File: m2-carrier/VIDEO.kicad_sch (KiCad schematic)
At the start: 8 parts, among them U7 AT7456E

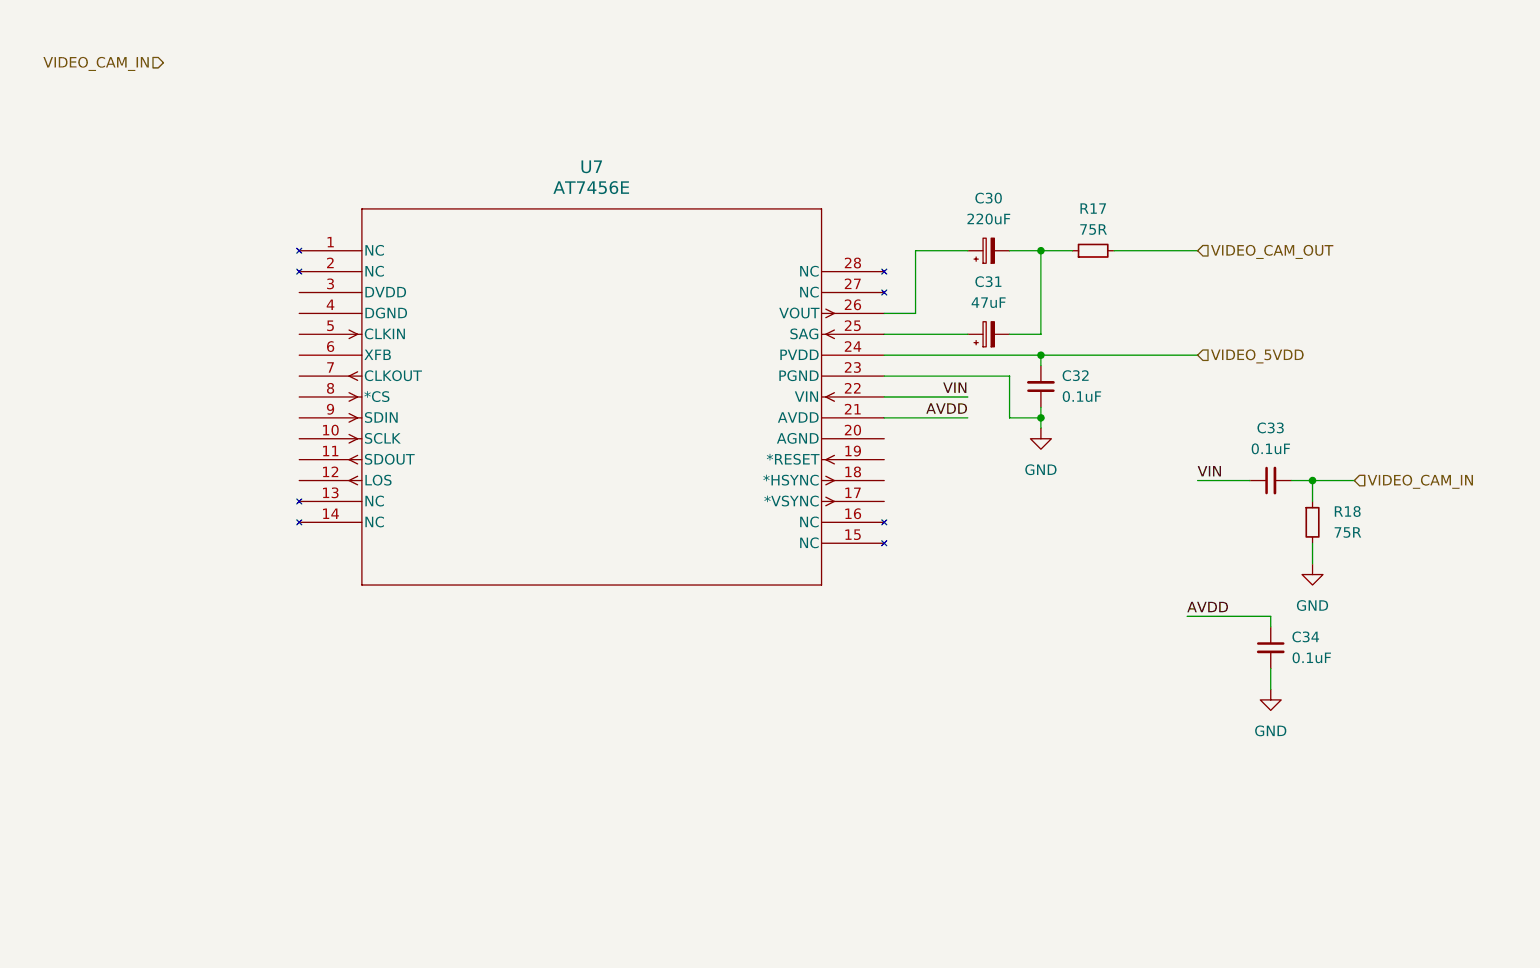
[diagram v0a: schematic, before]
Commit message: Populated OSD IC
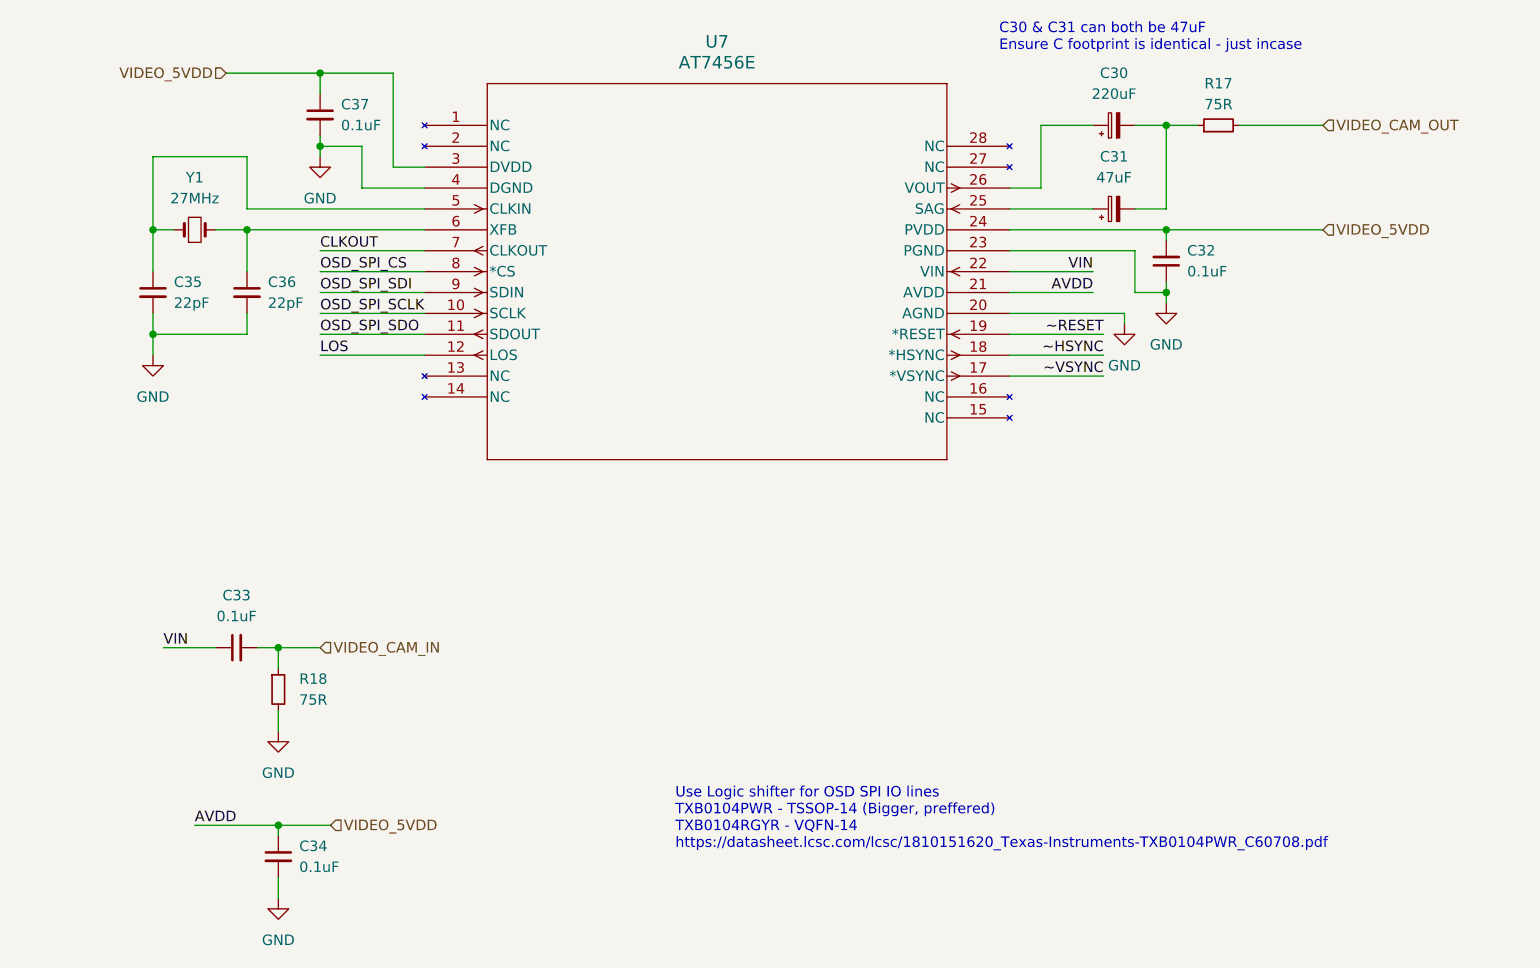
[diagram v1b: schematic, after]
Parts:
- added C35, C36: 22pF, symbol Device:C_Small
- added C37: 0.1uF, symbol Device:C_Small
- added Y1: 27MHz, symbol Device:Crystal_Small
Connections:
- net AVDD is gone; now on net VIDEO_5VDD: C34.1, U7.21 (AVDD)
- net GND: now also U7.20 (AGND), U7.4 (DGND), C35.2, C36.2, C37.2
- net VIDEO_5VDD: now also U7.3 (DVDD), C37.1
- net OSD_SPI_SCLK: now reaches U7.10 (SCLK)
- net OSD_SPI_SDO: now reaches U7.11 (SDOUT)
- net LOS: now reaches U7.12 (LOS)
- net ~VSYNC: now reaches U7.17 (*VSYNC)
- net ~HSYNC: now reaches U7.18 (*HSYNC)
- net ~RESET: now reaches U7.19 (*RESET)
- net at U7.5 (CLKIN): now also C35.1, Y1.1
- net at U7.6 (XFB): now also C36.1, Y1.2
- net CLKOUT: now reaches U7.7 (CLKOUT)
- net OSD_SPI_CS: now reaches U7.8 (*CS)
- net OSD_SPI_SDI: now reaches U7.9 (SDIN)
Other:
- note added: "C30 & C31 can both be 47uF Ensure C footprint is identical - just incase"
- note added: "Use Logic shifter for OSD SPI IO lines TXB0104PWR - TSSOP-14 (Bigger, preffered) TXB0104RGYR - VQFN-14 https://datasheet.lcsc.com/lcsc/1810151620_Texas-Instruments-TXB0104PWR_C60708.pdf"
- moved on the sheet: C30, C31, C32, C33, C34, R17, R18, U7

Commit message: Added base board
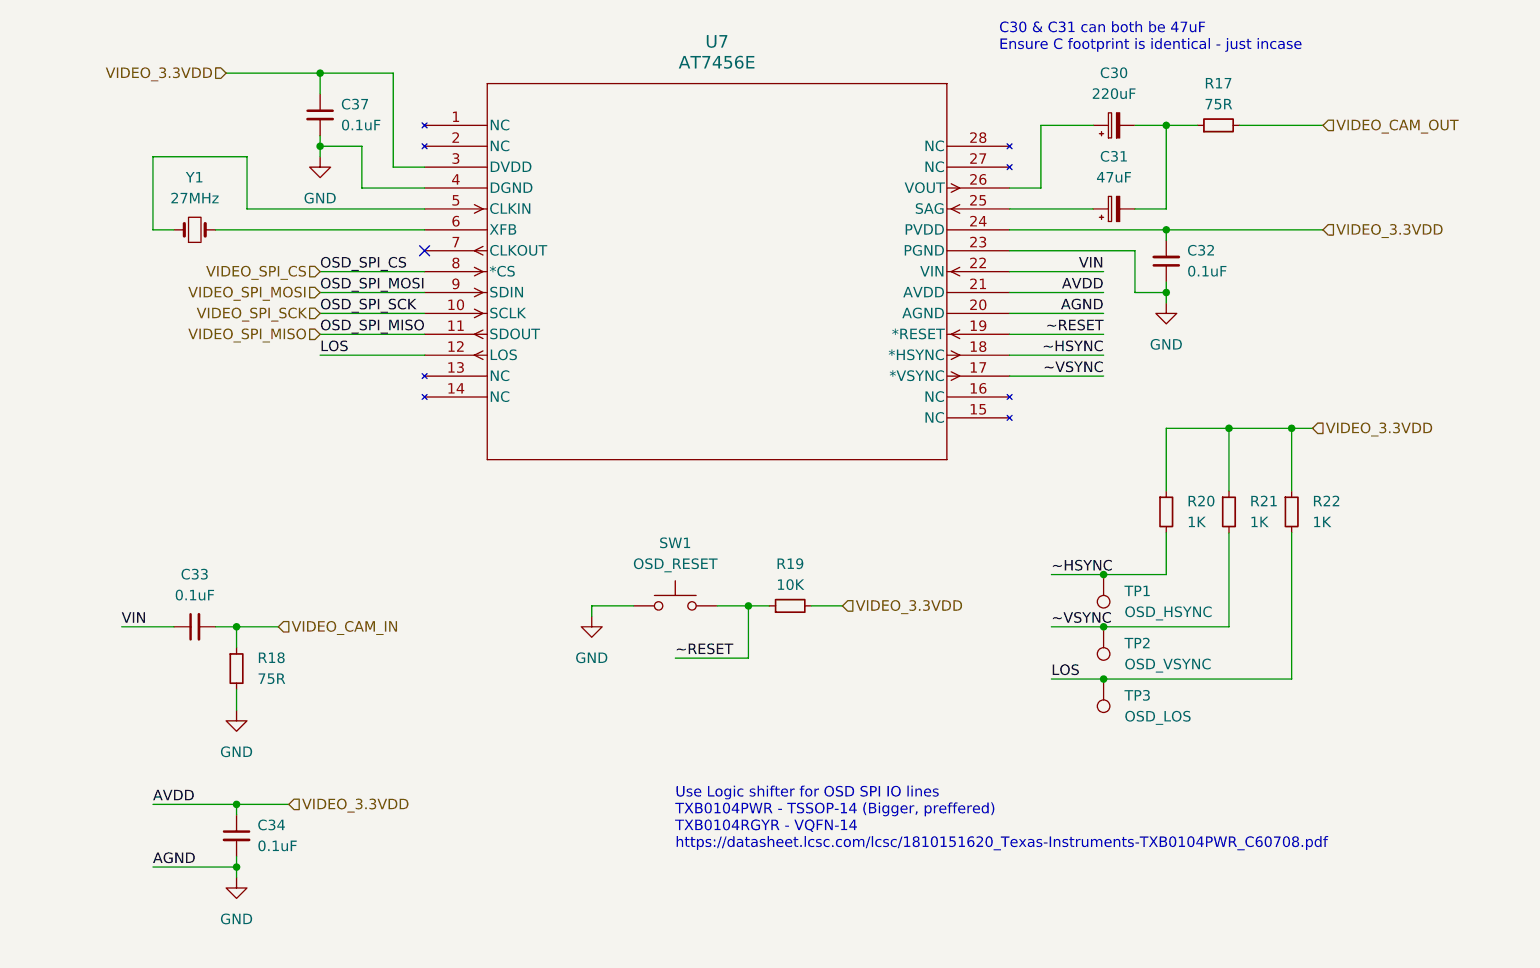
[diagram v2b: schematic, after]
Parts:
- removed C35, C36: 22pF, symbol Device:C_Small
- added R19: 10K, Resistor_SMD:R_0402_1005Metric, symbol Device:R_Small
- added R20, R21, R22: 1K, Resistor_SMD:R_0402_1005Metric, symbol Device:R_Small
- added SW1: OSD_RESET, Button_Switch_SMD:SW_SPST_PTS810, symbol Switch:SW_Push
- added TP1: OSD_HSYNC, symbol Connector:TestPoint
- added TP2: OSD_VSYNC, symbol Connector:TestPoint
- added TP3: OSD_LOS, symbol Connector:TestPoint
- C30: footprint (none) -> Capacitor_SMD:CP_Elec_6.3x5.4; LCSC (none) -> C72500
- C31: footprint (none) -> Capacitor_SMD:CP_Elec_6.3x5.4; LCSC (none) -> C72515
- C32, C33, C34, C37: footprint (none) -> Capacitor_SMD:C_0603_1608Metric
- R17, R18: footprint (none) -> Resistor_SMD:R_0402_1005Metric
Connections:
- net GND: now also SW1.1
- net LOS: now also R22.2, TP3.1
- net ~HSYNC: now also R20.2, TP1.1
- net ~RESET: now also R19.1, SW1.2
- net ~VSYNC: now also R21.2, TP2.1
- net CLKOUT: no longer names the net of U7.7 (CLKOUT)
- net OSD_SPI_CS renamed VIDEO_SPI_CS
- net OSD_SPI_SCLK renamed VIDEO_SPI_SCK
- net OSD_SPI_SDI renamed VIDEO_SPI_MOSI
- net OSD_SPI_SDO renamed VIDEO_SPI_MISO
- net VIDEO_5VDD renamed VIDEO_3.3VDD
- net VIDEO_3.3VDD: now also R19.2, R20.1, R21.1, R22.1
- no-connect marks 0 -> 1
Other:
- moved on the sheet: C33, C34, R18

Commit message: added stuff
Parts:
- removed TP1: OSD_HSYNC, symbol Connector:TestPoint
- removed TP2: OSD_VSYNC, symbol Connector:TestPoint
- removed TP3: OSD_LOS, symbol Connector:TestPoint
- U7: LCSC (none) -> C82351
- Y1: footprint (none) -> Crystal:Crystal_SMD_Abracon_ABM3-2Pin_5.0x3.2mm
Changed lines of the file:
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@@
   (junction (at 102.87 86.36) (diameter 0) (color 0 0 0 0)
   )
-  (junction (at 146.05 95.25) (diameter 0) (color 0 0 0 0)
-  )
   (junction (at 40.64 110.49) (diameter 0) (color 0 0 0 0)
   )
@@
   (junction (at 153.67 40.64) (diameter 0) (color 0 0 0 0)
   )
-  (junction (at 146.05 88.9) (diameter 0) (color 0 0 0 0)
-  )
   (junction (at 40.64 88.9) (diameter 0) (color 0 0 0 0)
-  )
-  (junction (at 146.05 82.55) (diameter 0) (color 0 0 0 0)
   )
   (junction (at 153.67 27.94) (diameter 0) (color 0 0 0 0)
@@
     (stroke (width 0) (type default))
   )
-  (wire (pts (xy 146.05 82.55) (xy 153.67 82.55))
-    (stroke (width 0) (type default))
-  )
   (wire (pts (xy 30.48 118.11) (xy 40.64 118.11))
     (stroke (width 0) (type default))
@@
     (stroke (width 0) (type default))
   )
-  (wire (pts (xy 146.05 95.25) (xy 168.91 95.25))
+  (wire (pts (xy 139.7 95.25) (xy 168.91 95.25))
     (stroke (width 0) (type default))
   )
@@
     (stroke (width 0) (type default))
   )
-  (wire (pts (xy 139.7 82.55) (xy 146.05 82.55))
+  (wire (pts (xy 139.7 82.55) (xy 153.67 82.55))
     (stroke (width 0) (type default))
   )
@@
     (stroke (width 0) (type default))
   )
-  (wire (pts (xy 146.05 88.9) (xy 161.29 88.9))
+  (wire (pts (xy 139.7 88.9) (xy 161.29 88.9))
     (stroke (width 0) (type default))
   )
@@
     (stroke (width 0) (type default))
   )
-  (wire (pts (xy 139.7 95.25) (xy 146.05 95.25))
-    (stroke (width 0) (type default))
-  )
   (wire (pts (xy 50.8 55.88) (xy 63.5 55.88))
     (stroke (width 0) (type default))
@@
   )
   (wire (pts (xy 83.82 86.36) (xy 88.9 86.36))
-    (stroke (width 0) (type default))
-  )
-  (wire (pts (xy 139.7 88.9) (xy 146.05 88.9))
     (stroke (width 0) (type default))
   )
@@
       (effects (font (size 1.27 1.27)))
     )
-    (property "Footprint" "" (at 35.56 40.64 0)
+    (property "Footprint" "Crystal:Crystal_SMD_Abracon_ABM3-2Pin_5.0x3.2mm" (at 35.56 40.64 0)
       (effects (font (size 1.27 1.27)) hide)
     )
@@
     )
   )
-  (symbol (lib_id "Connector:TestPoint") (at 146.05 95.25 180) (unit 1)
-    (in_bom yes) (on_board yes) (dnp no) (fields_autoplaced)
-    (property "Reference" "TP3" (at 148.59 97.282 0)
-      (effects (font (size 1.27 1.27)) (justify right))
-    )
-    (property "Value" "OSD_LOS" (at 148.59 99.822 0)
-      (effects (font (size 1.27 1.27)) (justify right))
-    )
-    (property "Footprint" "" (at 140.97 95.25 0)
-      (effects (font (size 1.27 1.27)) hide)
-    )
-    (property "Datasheet" "~" (at 140.97 95.25 0)
-      (effects (font (size 1.27 1.27)) hide)
-    )
-    (pin "1")
-    (instances
-      (project "m2-carrier"
-        (path "/5f2bc0b3-3222-4ac4-baca-7f43b47f8a71/2e07962d-b8cb-4e00-9dfe-2f6dcf47d665"
-          (reference "TP3") (unit 1)
-        )
-      )
-    )
-  )
   (symbol (lib_id "2023-11-30_12-19-21:max7456eui+") (at 63.5 27.94 0) (unit 1)
     (in_bom yes) (on_board yes) (dnp no) (fields_autoplaced)
@@
     )
     (property "Schematic" "https://github.com/Arduinolibrary/DFRobot_FireBeetle_OSD_Module/raw/master/FireBeetle%20OSD%20Character%20Overlay%20Module%20Schematic.pdf" (at 63.5 27.94 0)
+      (effects (font (size 1.27 1.27)) hide)
+    )
+    (property "LCSC" "C82351" (at 63.5 27.94 0)
       (effects (font (size 1.27 1.27)) hide)
     )
@@
     )
   )
-  (symbol (lib_id "Connector:TestPoint") (at 146.05 82.55 180) (unit 1)
-    (in_bom yes) (on_board yes) (dnp no) (fields_autoplaced)
-    (property "Reference" "TP1" (at 148.59 84.582 0)
-      (effects (font (size 1.27 1.27)) (justify right))
-    )
-    (property "Value" "OSD_HSYNC" (at 148.59 87.122 0)
-      (effects (font (size 1.27 1.27)) (justify right))
-    )
-    (property "Footprint" "" (at 140.97 82.55 0)
-      (effects (font (size 1.27 1.27)) hide)
-    )
-    (property "Datasheet" "~" (at 140.97 82.55 0)
-      (effects (font (size 1.27 1.27)) hide)
-    )
-    (pin "1")
-    (instances
-      (project "m2-carrier"
-        (path "/5f2bc0b3-3222-4ac4-baca-7f43b47f8a71/2e07962d-b8cb-4e00-9dfe-2f6dcf47d665"
-          (reference "TP1") (unit 1)
-        )
-      )
-    )
-  )
   (symbol (lib_id "Device:R_Small") (at 40.64 93.98 0) (unit 1)
     (in_bom yes) (on_board yes) (dnp no) (fields_autoplaced)
@@
         )
       )
-    )
-  )
-  (symbol (lib_id "Connector:TestPoint") (at 146.05 88.9 180) (unit 1)
-    (in_bom yes) (on_board yes) (dnp no) (fields_autoplaced)
-    (property "Reference" "TP2" (at 148.59 90.932 0)
-      (effects (font (size 1.27 1.27)) (justify right))
-    )
-    (property "Value" "OSD_VSYNC" (at 148.59 93.472 0)
-      (effects (font (size 1.27 1.27)) (justify right))
-    )
-    (property "Footprint" "" (at 140.97 88.9 0)
-      (effects (font (size 1.27 1.27)) hide)
-    )
-    (property "Datasheet" "~" (at 140.97 88.9 0)
-      (effects (font (size 1.27 1.27)) hide)
-    )
-    (pin "1")
-    (instances
-      (project "m2-carrier"
-        (path "/5f2bc0b3-3222-4ac4-baca-7f43b47f8a71/2e07962d-b8cb-4e00-9dfe-2f6dcf47d665"
-          (reference "TP2") (unit 1)
-        )
-      )
